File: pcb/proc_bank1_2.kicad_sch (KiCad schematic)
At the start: 3 parts, among them U1 XC6SLX16-FTG256, U14 ECS-7050MV

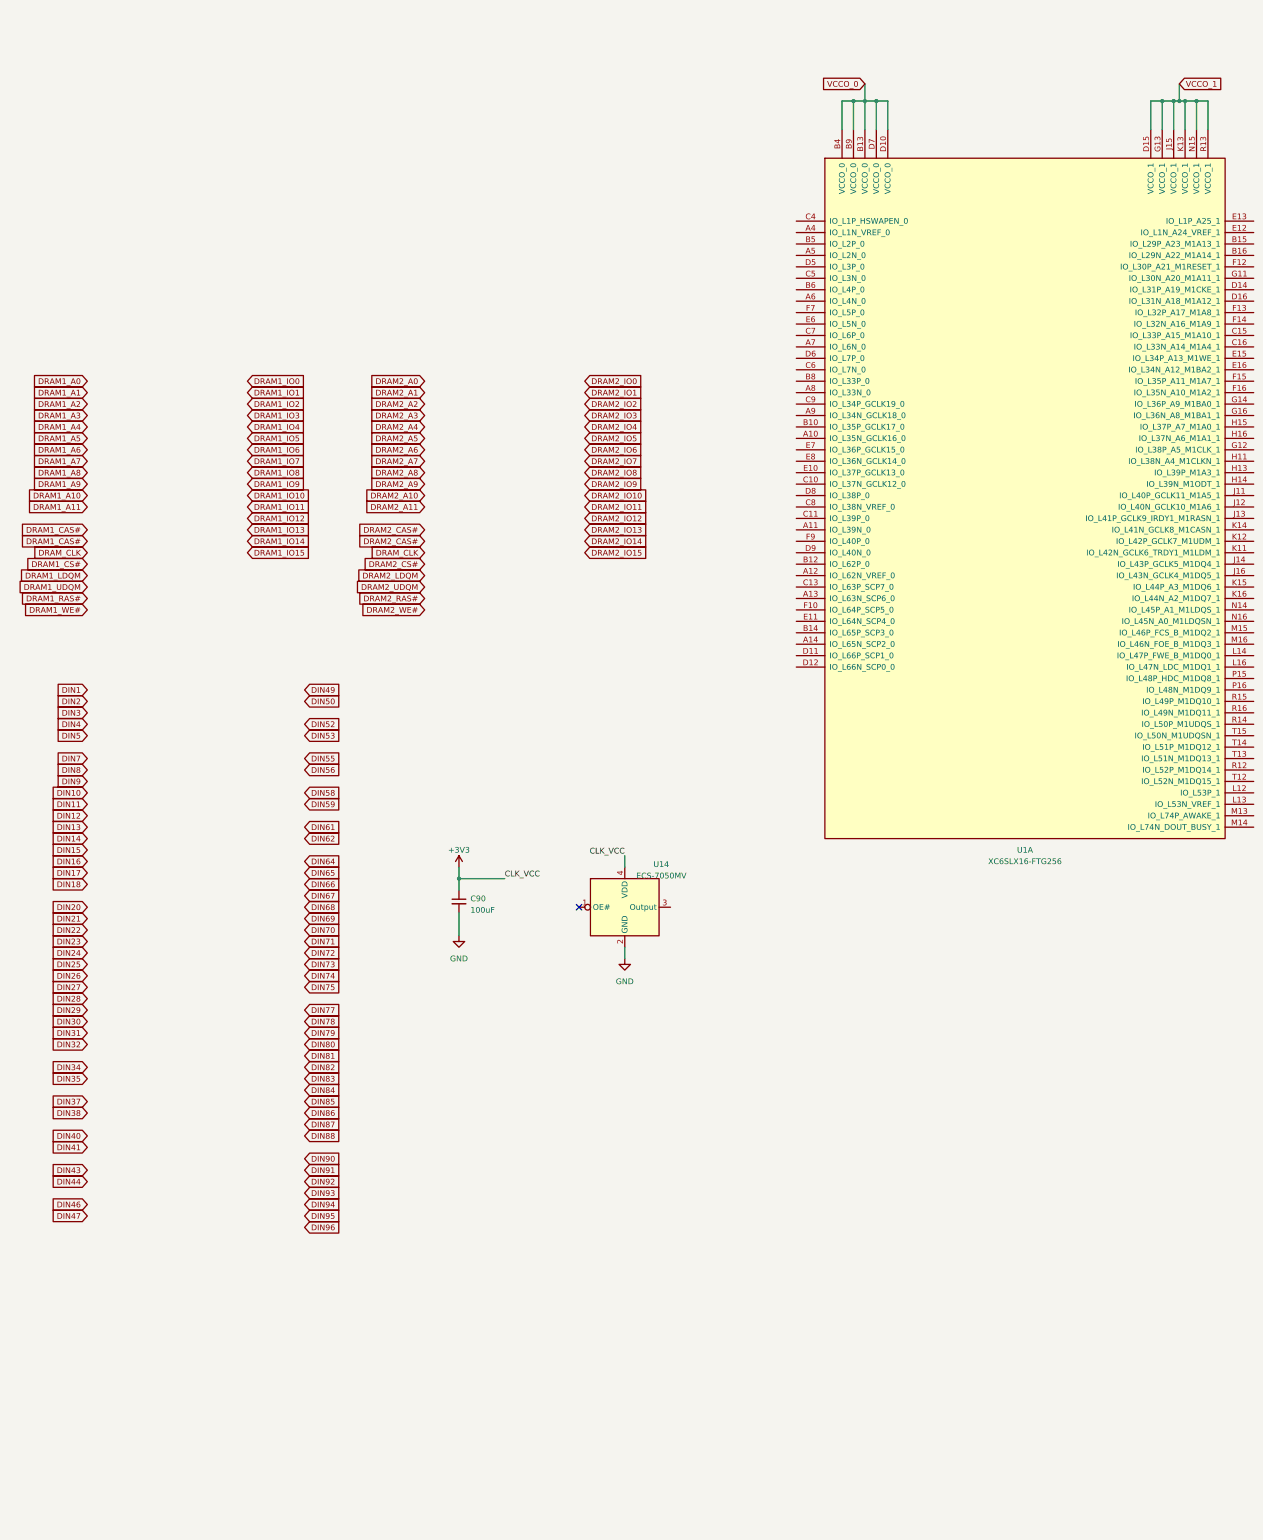
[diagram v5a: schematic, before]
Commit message: change to lx9 and reduce power
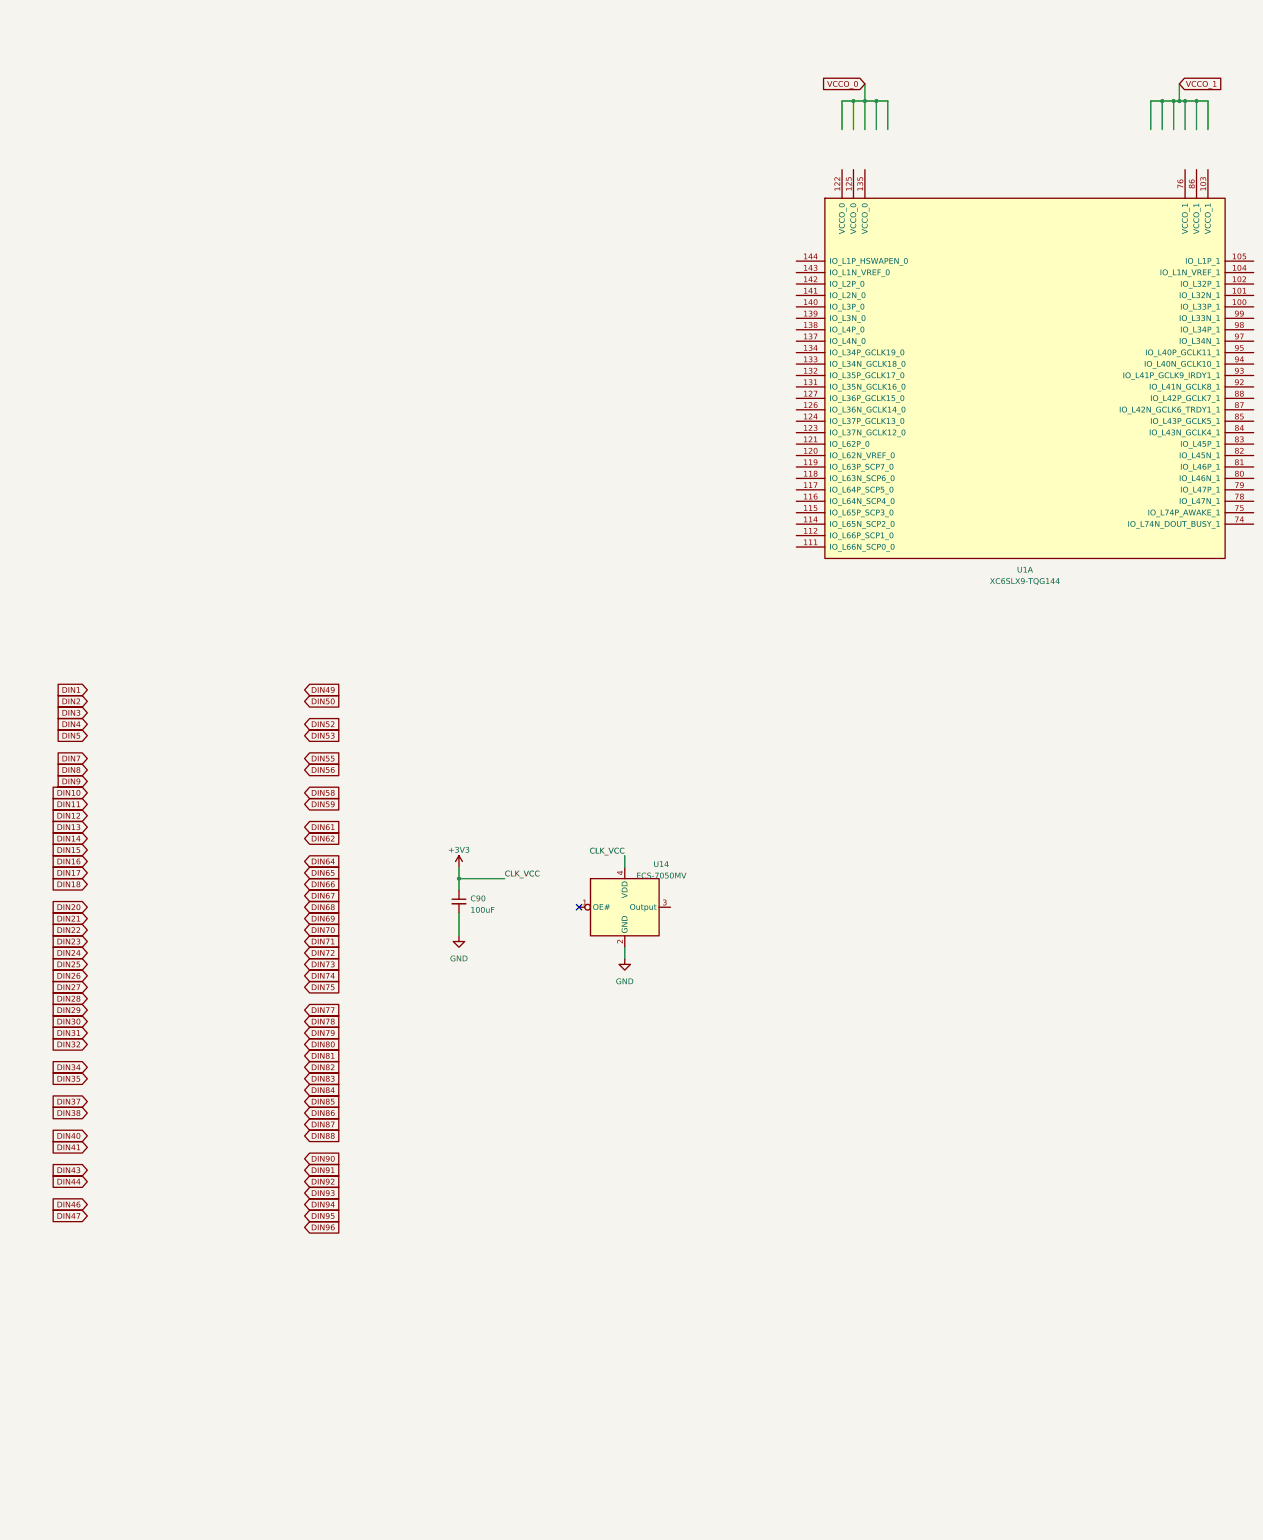
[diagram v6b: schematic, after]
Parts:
- removed U1: XC6SLX16-FTG256, Package_BGA:Xilinx_FTG256, symbol FPGA_Xilinx_Spartan6:XC6SLX16-FTG256
- added U1: XC6SLX9-TQG144, Package_QFP:TQFP-144_20x20mm_P0.5mm, symbol FPGA_Xilinx_Spartan6:XC6SLX9-TQG144

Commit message: route pol
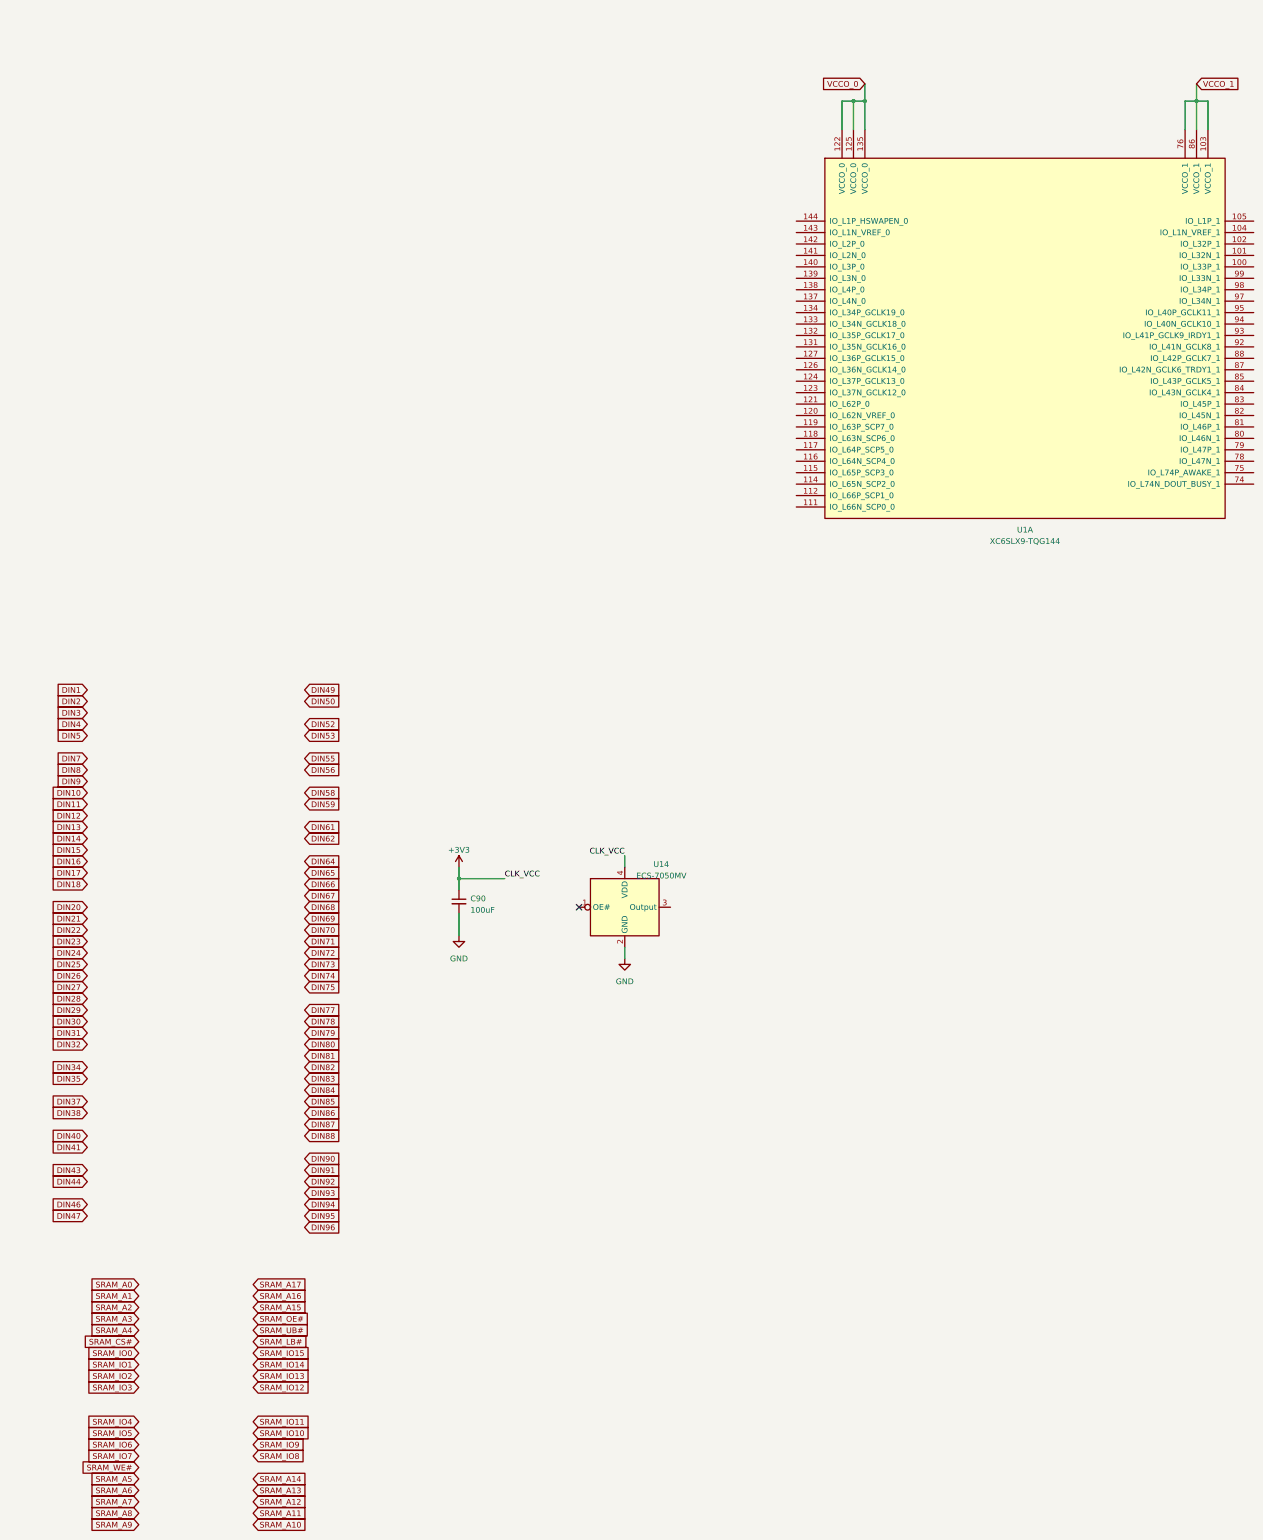
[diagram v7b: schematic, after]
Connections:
- net VCCO_0: now also U1.122 (VCCO_0), U1.125 (VCCO_0), U1.135 (VCCO_0)
- net VCCO_1: now also U1.103 (VCCO_1), U1.76 (VCCO_1), U1.86 (VCCO_1)
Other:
- moved on the sheet: U1A
